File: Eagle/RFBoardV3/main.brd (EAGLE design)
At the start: 34.3 x 77.5 mm, 24 parts, among them Q1 8/16/20MHz, U1 ATMEGA328

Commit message: Reasonator to top, and added 10k resistor
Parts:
- added R3: 10K, SparkFun:0603-RES
- moved Q1 0.80 mm to (26.1, 7.05), flipped to the top, turned to 45 degrees
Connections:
- new net N$6: R3.1, T1.2
- net N$3: now also R3.2; no longer T1.2
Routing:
- net N$3: track 92.2 -> 4.82 mm
- net N$6: track 0.00 -> 85.7 mm
- net GND: track 82.0 -> 84.0 mm, vias 10 -> 9
- net N$1: track 2.13 -> 2.96 mm, vias 1 -> 0
- net N$2: track 1.92 -> 2.29 mm, vias 1 -> 0
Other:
- board text added: "MicroRF V3.1"
- board text removed: "MicroRF V3"
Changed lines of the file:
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@@
 <text x="32.512" y="48.895" size="1.778" layer="21" rot="R90">REED</text>
 <text x="15.8496" y="0.3556" size="0.8128" layer="21" font="fixed" ratio="15">DTR</text>
-<text x="28.0035" y="37.1475" size="0.8128" layer="21" ratio="15" rot="R270">MicroRF V3</text>
+<text x="28.0035" y="37.1475" size="0.8128" layer="21" ratio="15" rot="R270">MicroRF V3.1</text>
 <text x="31.115" y="67.6275" size="1.016" layer="21">D5</text>
 <text x="31.0515" y="4.7625" size="0.8128" layer="22" ratio="15" rot="MR90">VCC</text>
@@
 <element name="C2" library="SparkFun" package="0603-CAP" value="0.1uF" x="8.9281" y="14.7955" rot="R180"/>
 <element name="S1" library="Testing" package="TACTILE-SWITCH-SMD-ALT01" value="Reset" x="31.1785" y="21.7805" rot="R270"/>
-<element name="Q1" library="Testing" package="RESONATOR-SMD-1:1" value="8/16/20MHz" x="25.3371375" y="7.08378125" rot="MR135"/>
+<element name="Q1" library="Testing" package="RESONATOR-SMD-1:1" value="8/16/20MHz" x="26.13378125" y="7.0478625" rot="R45"/>
 <element name="BATPLUS" library="pinhead" package="1X01" value="" x="6.35" y="25.4" smashed="yes">
 <attribute name="NAME" x="9.7663" y="27.2288" size="1.27" layer="26" ratio="10" rot="MR0"/>
@@
 <attribute name="VALUE" x="21.9675" y="3.13" size="1.016" layer="27" rot="R90"/>
 </element>
+<element name="R3" library="SparkFun" package="0603-RES" value="10K" x="27.94" y="56.8325" rot="R90"/>
 </elements>
 <signals>
@@
 <vertex x="34.29" y="41.91"/>
 </polygon>
-<via x="18.7325" y="40.64" extent="1-16" drill="0.6"/>
+<via x="27.6225" y="5.715" extent="1-16" drill="0.6"/>
 <via x="21.2725" y="40.64" extent="1-16" drill="0.6"/>
 <via x="27.94" y="40.64" extent="1-16" drill="0.6"/>
@@
 <wire x1="24.13" y1="25.0825" x2="23.8125" y2="25.4" width="0.4064" layer="1"/>
 <wire x1="23.8125" y1="25.4" x2="19.05" y2="25.4" width="0.4064" layer="1"/>
-<via x="21.844" y="4.8895" extent="1-16" drill="0.6"/>
 <wire x1="33.147" y1="24.5364" x2="33.147" y2="19.05" width="0.4064" layer="1"/>
 <wire x1="33.147" y1="19.05" x2="33.0835" y2="18.9865" width="0.4064" layer="1"/>
@@
 <wire x1="32.6898" y1="15.9258" x2="30.2133" y2="15.9258" width="0.4064" layer="1"/>
 <wire x1="30.2133" y1="15.9258" x2="30.1625" y2="15.875" width="0.4064" layer="1"/>
+<wire x1="27.5844" y1="5.715" x2="26.9748" y2="6.3246" width="0.254" layer="1"/>
+<wire x1="26.9748" y1="6.3246" x2="26.13378125" y2="7.0478625" width="0.254" layer="1"/>
+<wire x1="27.5844" y1="5.715" x2="27.6225" y2="5.715" width="0.254" layer="1"/>
 </signal>
 <signal name="AREF">
@@
 <contactref element="U1" pad="8"/>
 <contactref element="Q1" pad="3"/>
-<wire x1="24.9936" y1="9.0678" x2="23.5458" y2="9.0678" width="0.1524" layer="1"/>
-<wire x1="25.3746" y1="8.6868" x2="24.9936" y2="9.0678" width="0.1524" layer="16"/>
+<wire x1="25.8318" y1="9.0678" x2="23.5458" y2="9.0678" width="0.1524" layer="1"/>
+<wire x1="26.2128" y1="8.6868" x2="25.8318" y2="9.0678" width="0.1524" layer="1"/>
 <wire x1="23.5458" y1="9.0678" x2="23.505940625" y2="9.090484375" width="0.1524" layer="1"/>
-<wire x1="25.3746" y1="8.6868" x2="25.467246875" y2="8.650728125" width="0.1524" layer="16"/>
-<via x="24.9936" y="9.0678" extent="1-16" drill="0.3302"/>
+<wire x1="26.2128" y1="8.6868" x2="26.2638875" y2="8.614809375" width="0.1524" layer="1"/>
 </signal>
 <signal name="N$2">
 <contactref element="U1" pad="7"/>
 <contactref element="Q1" pad="1"/>
-<wire x1="23.7744" y1="7.6962" x2="23.0124" y2="8.4582" width="0.1524" layer="1"/>
-<wire x1="23.7744" y1="7.0104" x2="23.7744" y2="7.6962" width="0.1524" layer="16"/>
+<wire x1="24.5364" y1="6.9342" x2="23.0124" y2="8.4582" width="0.1524" layer="1"/>
 <wire x1="23.0124" y1="8.4582" x2="22.940253125" y2="8.524796875" width="0.1524" layer="1"/>
-<wire x1="23.7744" y1="7.0104" x2="23.770190625" y2="6.953671875" width="0.1524" layer="16"/>
-<via x="23.7744" y="7.6962" extent="1-16" drill="0.3302"/>
+<wire x1="24.5364" y1="6.9342" x2="24.56683125" y2="6.917753125" width="0.1524" layer="1"/>
 </signal>
 <signal name="DTR">
@@
 <signal name="N$3">
 <contactref element="D2--A0" pad="1"/>
+<contactref element="R3" pad="2"/>
+<wire x1="27.9654" y1="61.5696" x2="27.9654" y2="57.6834" width="0.1524" layer="1"/>
+<wire x1="28.575" y1="62.1792" x2="27.9654" y2="61.5696" width="0.1524" layer="1"/>
+<wire x1="27.9654" y1="57.6834" x2="27.94" y2="57.6825" width="0.1524" layer="1"/>
+<wire x1="28.575" y1="62.1792" x2="28.575" y2="62.23" width="0.1524" layer="1"/>
+</signal>
+<signal name="N$5">
+<wire x1="20.955" y1="6.0325" x2="20.955" y2="5.715" width="0.4064" layer="1"/>
+<wire x1="20.955" y1="5.715" x2="21.9075" y2="4.7625" width="0.4064" layer="1"/>
+</signal>
+<signal name="N$6">
 <contactref element="T1" pad="2"/>
+<contactref element="R3" pad="1"/>
 <wire x1="17.2974" y1="1.2192" x2="21.4884" y2="1.2192" width="0.1524" layer="1"/>
 <wire x1="16.8402" y1="0.762" x2="17.2974" y2="1.2192" width="0.1524" layer="1"/>
 <wire x1="3.7338" y1="0.762" x2="16.8402" y2="0.762" width="0.1524" layer="1"/>
 <wire x1="0.8382" y1="3.6576" x2="3.7338" y2="0.762" width="0.1524" layer="1"/>
-<wire x1="0.8382" y1="34.4424" x2="0.8382" y2="3.6576" width="0.1524" layer="1"/>
-<wire x1="28.575" y1="62.1792" x2="0.8382" y2="34.4424" width="0.1524" layer="1"/>
+<wire x1="0.8382" y1="28.8798" x2="0.8382" y2="3.6576" width="0.1524" layer="1"/>
+<wire x1="27.8892" y1="55.9308" x2="0.8382" y2="28.8798" width="0.1524" layer="1"/>
 <wire x1="21.4884" y1="1.2192" x2="21.5375" y2="1.255" width="0.1524" layer="1"/>
-<wire x1="28.575" y1="62.1792" x2="28.575" y2="62.23" width="0.1524" layer="1"/>
-</signal>
-<signal name="N$5">
-<wire x1="20.955" y1="6.0325" x2="20.955" y2="5.715" width="0.4064" layer="1"/>
-<wire x1="20.955" y1="5.715" x2="21.9075" y2="4.7625" width="0.4064" layer="1"/>
+<wire x1="27.8892" y1="55.9308" x2="27.94" y2="55.9825" width="0.1524" layer="1"/>
 </signal>
 </signals>

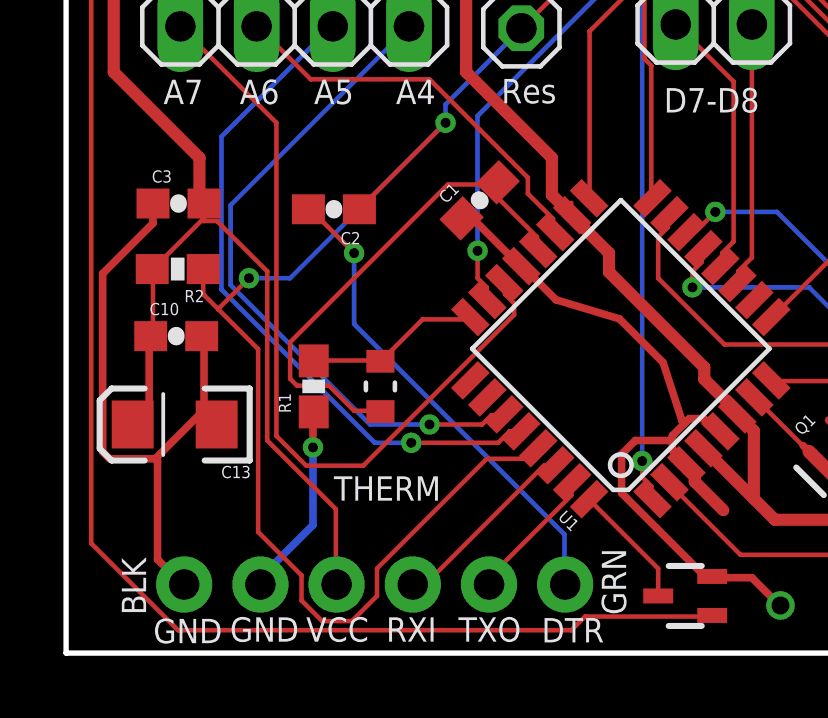
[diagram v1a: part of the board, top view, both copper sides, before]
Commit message: Reversed thermister and resistor
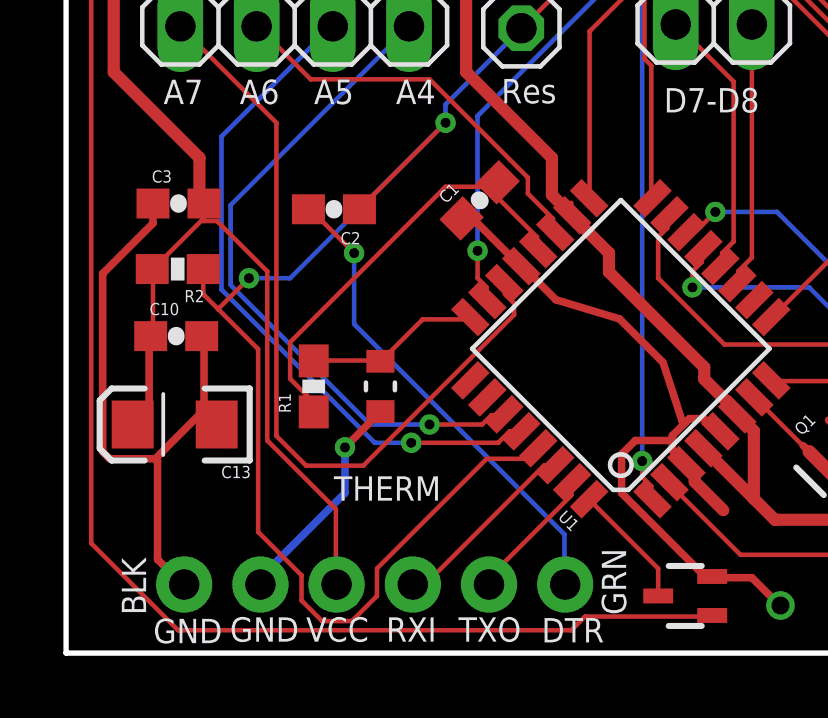
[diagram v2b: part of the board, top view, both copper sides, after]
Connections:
- net AREF: now also R1.1; no longer THERM.2
- net GND: now also THERM.2; no longer R1.1
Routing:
- net AREF: track 16.6 -> 14.6 mm
- net GND: track 84.0 -> 85.0 mm
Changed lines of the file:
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@@
 <?xml version="1.0" encoding="utf-8"?>
 <!DOCTYPE eagle SYSTEM "eagle.dtd">
-<eagle version="7.1.0">
+<eagle version="7.2.0">
 <drawing>
 <settings>
@@
 <wire x1="15.200065625" y1="12.90795625" x2="15.17254375" y2="12.89839375" width="0.254" layer="1"/>
 <wire x1="20.5343375" y1="7.735328125" x2="20.6151625" y2="7.65450625" width="0.254" layer="1"/>
-<contactref element="R1" pad="1"/>
 <contactref element="JP5" pad="9"/>
 <contactref element="T1" pad="3"/>
@@
 <wire x1="30.48" y1="3.048" x2="30.48" y2="3.0868" width="0.254" layer="1"/>
 <wire x1="32.6898" y1="2.286" x2="32.7025" y2="2.2225" width="0.254" layer="1"/>
-<wire x1="8.2296" y1="6.858" x2="8.2296" y2="8.001" width="0.254" layer="1"/>
-<wire x1="8.2296" y1="4.2672" x2="8.2296" y2="6.858" width="0.254" layer="16"/>
-<wire x1="6.477" y1="2.5146" x2="8.2296" y2="4.2672" width="0.254" layer="16"/>
-<wire x1="8.2296" y1="8.001" x2="8.255" y2="8.04" width="0.254" layer="1"/>
-<wire x1="6.477" y1="2.5146" x2="6.477" y2="2.286" width="0.254" layer="16"/>
 <wire x1="32.6898" y1="15.9258" x2="32.7025" y2="15.875" width="0.254" layer="1"/>
 <wire x1="3.048" y1="3.1242" x2="3.048" y2="6.4008" width="0.254" layer="1"/>
@@
 <wire x1="3.048" y1="6.4008" x2="2.9718" y2="6.477" width="0.254" layer="1"/>
 <wire x1="3.8862" y1="2.286" x2="3.937" y2="2.286" width="0.254" layer="1"/>
-<via x="8.2296" y="6.858" extent="1-16" drill="0.3302"/>
 <wire x1="33.0708" y1="18.9738" x2="33.0835" y2="18.9865" width="0.254" layer="1"/>
 <wire x1="32.766" y1="16.002" x2="32.7025" y2="15.875" width="0.254" layer="1"/>
@@
 <wire x1="26.9748" y1="6.3246" x2="26.13378125" y2="7.0478625" width="0.254" layer="1"/>
 <wire x1="27.5844" y1="5.715" x2="27.6225" y2="5.715" width="0.254" layer="1"/>
+<contactref element="THERM" pad="2"/>
+<wire x1="9.2964" y1="6.858" x2="10.4394" y2="8.001" width="0.254" layer="1"/>
+<wire x1="9.2964" y1="5.334" x2="9.2964" y2="6.858" width="0.254" layer="16"/>
+<wire x1="6.477" y1="2.5146" x2="9.2964" y2="5.334" width="0.254" layer="16"/>
+<wire x1="10.4394" y1="8.001" x2="10.4775" y2="8.0518" width="0.254" layer="1"/>
+<wire x1="6.477" y1="2.5146" x2="6.477" y2="2.286" width="0.254" layer="16"/>
+<via x="9.2964" y="6.858" extent="1-16" drill="0.3302"/>
 </signal>
 <signal name="AREF">
 <contactref element="C1" pad="2"/>
 <contactref element="U1" pad="20"/>
-<contactref element="THERM" pad="2"/>
-<wire x1="9.6012" y1="8.0772" x2="10.4394" y2="8.0772" width="0.1524" layer="1"/>
-<wire x1="8.763" y1="8.9154" x2="9.6012" y2="8.0772" width="0.1524" layer="1"/>
-<wire x1="7.6962" y1="8.9154" x2="8.763" y2="8.9154" width="0.1524" layer="1"/>
-<wire x1="7.4676" y1="9.144" x2="7.6962" y2="8.9154" width="0.1524" layer="1"/>
-<wire x1="7.4676" y1="10.3632" x2="7.4676" y2="9.144" width="0.1524" layer="1"/>
-<wire x1="12.7254" y1="15.621" x2="7.4676" y2="10.3632" width="0.1524" layer="1"/>
-<wire x1="14.3256" y1="15.621" x2="12.7254" y2="15.621" width="0.1524" layer="1"/>
-<wire x1="10.4394" y1="8.0772" x2="10.4775" y2="8.0518" width="0.1524" layer="1"/>
-<wire x1="14.3256" y1="15.621" x2="14.38824375" y2="15.6941625" width="0.1524" layer="1"/>
 <wire x1="15.6972" y1="13.8684" x2="15.6972" y2="13.4874" width="0.1524" layer="1"/>
 <wire x1="14.3256" y1="15.24" x2="15.6972" y2="13.8684" width="0.1524" layer="1"/>
@@
 <wire x1="15.6972" y1="13.4874" x2="15.73823125" y2="13.46408125" width="0.1524" layer="1"/>
 <wire x1="14.3256" y1="15.5448" x2="14.38824375" y2="15.6941625" width="0.1524" layer="1"/>
+<contactref element="R1" pad="1"/>
+<wire x1="8.2296" y1="8.382" x2="8.2296" y2="8.0772" width="0.1524" layer="1"/>
+<wire x1="7.4676" y1="9.144" x2="8.2296" y2="8.382" width="0.1524" layer="1"/>
+<wire x1="7.4676" y1="10.3632" x2="7.4676" y2="9.144" width="0.1524" layer="1"/>
+<wire x1="12.6492" y1="15.5448" x2="7.4676" y2="10.3632" width="0.1524" layer="1"/>
+<wire x1="14.2494" y1="15.5448" x2="12.6492" y2="15.5448" width="0.1524" layer="1"/>
+<wire x1="8.2296" y1="8.0772" x2="8.255" y2="8.04" width="0.1524" layer="1"/>
+<wire x1="14.2494" y1="15.5448" x2="14.38824375" y2="15.6941625" width="0.1524" layer="1"/>
 </signal>
 <signal name="RESET">
